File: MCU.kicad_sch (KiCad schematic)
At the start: 18 parts, among them J1 FTSH-105-01-L-DV, SW1 SW_Push, Y1 8MHz, Y2 32KHz

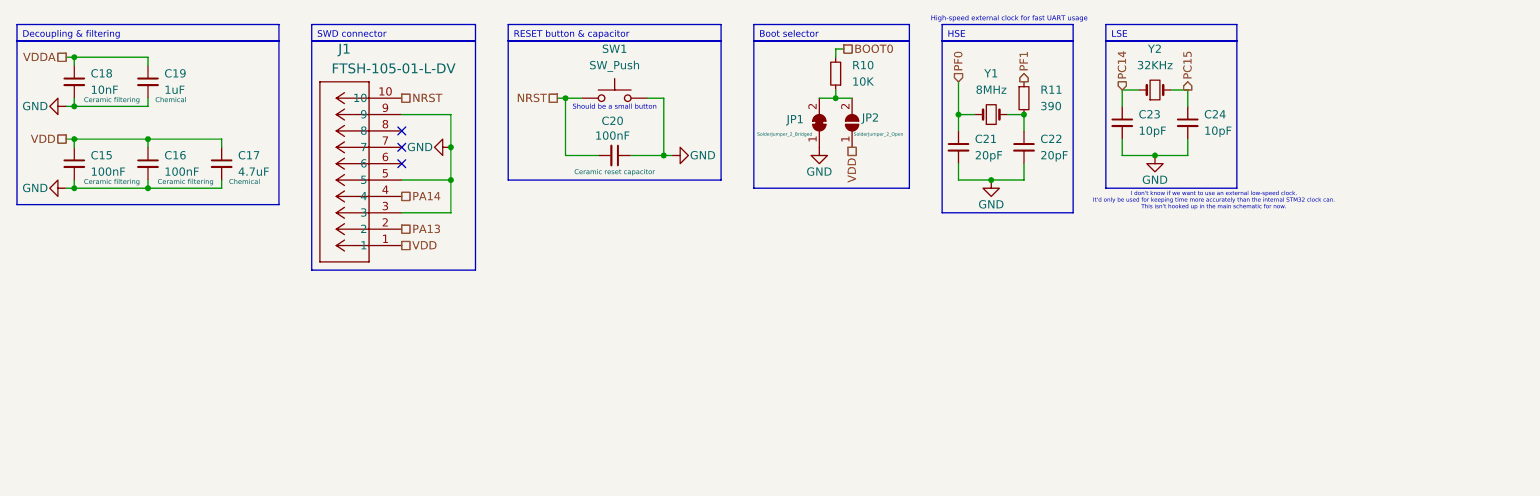
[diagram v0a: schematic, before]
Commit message: Haven't checked LSE, NRST, BOOT0 and SWD
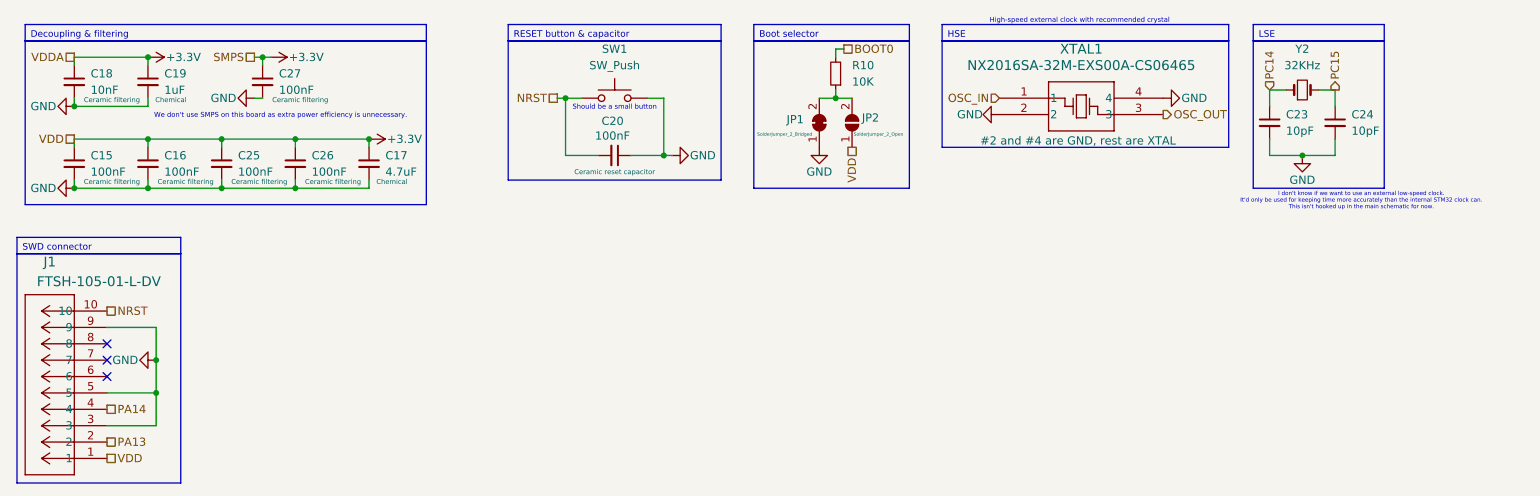
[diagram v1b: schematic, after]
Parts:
- removed C21, C22: 20pF, symbol Device:C_Small
- removed R11: 390, symbol Device:R_Small
- removed Y1: 8MHz, symbol Device:Crystal_Small
- added C25, C26, C27: 100nF, symbol Device:C_Small
- added XTAL1: NX2016SA-32M-EXS00A-CS06465, NX2016SA_NDK, symbol NX2016SA-32M-EXS00A-CS06465:NX2016SA-32M-EXS00A-CS06465
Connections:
- net VDDA is gone; now on net +3.3V: C18.1, C19.1
- net GND: now also C25.2, C26.2, C27.2, XTAL1.2, XTAL1.4
- net VDD renamed +3.3V
- net +3.3V: now also C25.1, C26.1, C27.1
- new net OSC_IN: XTAL1.1
- new net OSC_OUT: XTAL1.3
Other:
- note added: "High-speed external clock with recommended crystal"
- note added: "We don't use SMPS on this board as extra power efficiency is unnecessary."
- note removed: "High-speed external clock for fast UART usage"
- moved on the sheet: C17, C23, C24, J1, Y2
